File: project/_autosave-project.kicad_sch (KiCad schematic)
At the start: 6 parts, among them J1 Conn_02x16_Odd_Even, J2 USB_C_Receptacle_PowerOnly_6P, SW1 SS-12D10L9, U2 CH224K

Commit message: USB and PD circuit
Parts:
- added C1: 1u, symbol Device:C_Small
- added R1: 1K, symbol Device:R
- added R2: 10K, symbol Device:R
- added TP3: TestPoint_2Pole, symbol Connector:TestPoint_2Pole
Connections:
- net GND: now also J2.A12 (GND), J2.B12 (GND), U2.11 (GND), U2.2 (CFG2), U2.3 (CFG3), U2.9 (CFG1), C1.2
- net at J2.A5 (CC1): now also U2.7 (CC1)
- net at J2.A9 (VBUS), J2.B9 (VBUS): now also R1.2, R2.2
- net at J2.B5 (CC2): now also U2.6 (CC2)
- net VDD: now reaches U2.1 (VDD)
- net VDD: now also C1.1, R1.1
- net at U2.4 (DP): now also TP3.2
- net at U2.5 (DM): now also TP3.1
- net at U2.8 (VBUS): now also R2.1
- no-connect marks 1 -> 2
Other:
- note added: "Double pole TP added( if DM/DP needs to be shorted)"
- note added: "USB Type C and PD circuit"
- moved on the sheet: J2, U2

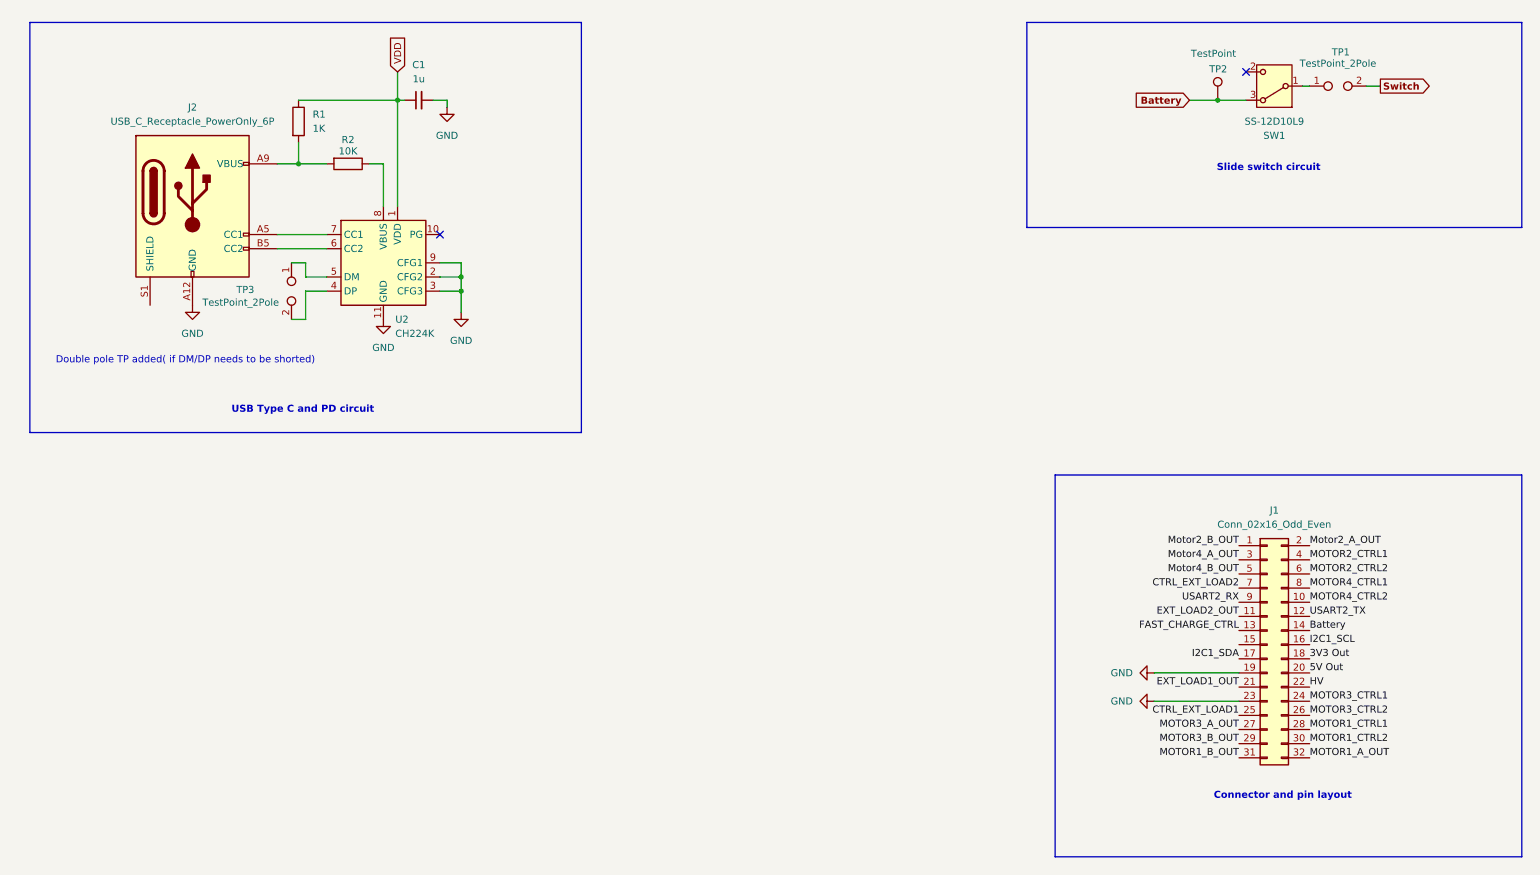
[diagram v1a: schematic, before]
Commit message: Add switching circuits
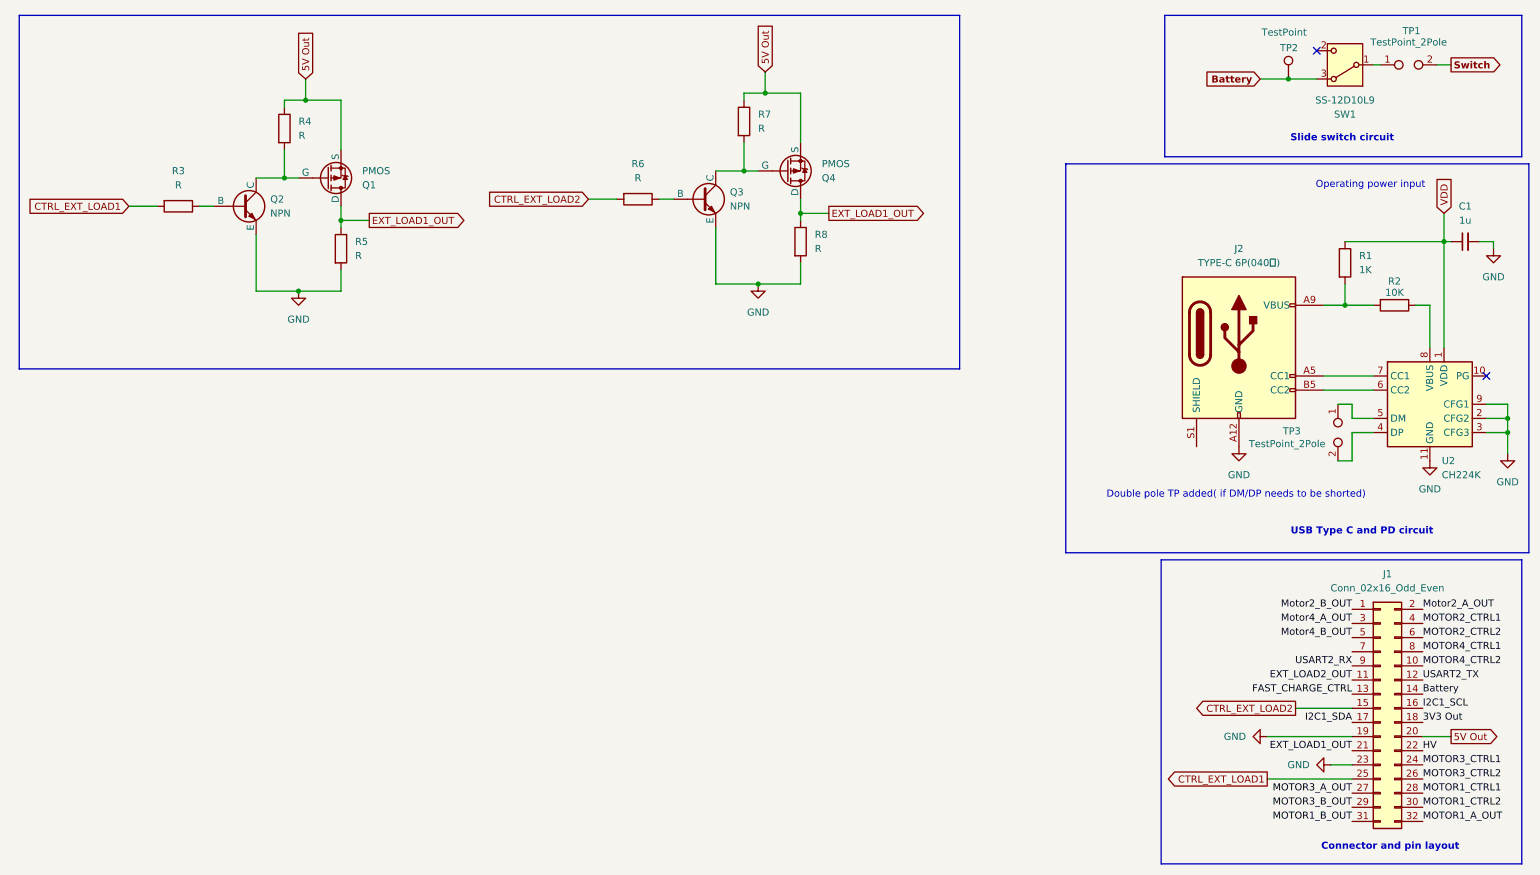
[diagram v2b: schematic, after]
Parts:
- added Q1, Q4: PMOS, symbol Simulation_SPICE:PMOS
- added Q2, Q3: NPN, symbol Simulation_SPICE:NPN
- added R3, R4, R5, R6, R7, R8: R, symbol Device:R
- J2: value USB_C_Receptacle_PowerOnly_6P -> TYPE-C 6P(040新)
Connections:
- net 5V Out: now also Q1.3 (S), Q4.3 (S), R4.1, R7.1
- net CTRL_EXT_LOAD1: now also R3.2
- net CTRL_EXT_LOAD2: now also J1.15 (Pin_15), R6.2; no longer J1.7 (Pin_7)
- net EXT_LOAD1_OUT: now also Q1.1 (D), Q4.1 (D), R5.1, R8.1
- net GND: now also Q2.3 (E), Q3.3 (E), R5.2, R8.2
- new net: Q1.2 (G), Q2.1 (C), R4.2
- new net: Q2.2 (B), R3.1
- new net: Q3.2 (B), R6.1
- new net: Q3.1 (C), Q4.2 (G), R7.2
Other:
- note added: "Operating power input"
- moved on the sheet: C1, J1, J2, R1, R2, SW1, TP1, TP2, TP3, U2

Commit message: Update _autosave-project.kicad_sch
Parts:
- renumbered R5 to R_L1, R8 to R_L2
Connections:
- net CTRL_EXT_LOAD2: now also J1.7 (Pin_7); no longer J1.15 (Pin_15)
- net EXT_LOAD1_OUT: no longer Q4.1 (D), R_L2.1
- net EXT_LOAD2_OUT: now also Q4.1 (D), R_L2.1
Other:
- note added: "External Load Switching circuits"
- note added: "Switch input?"
- moved on the sheet: Q1, Q2, Q3, Q4, R3, R4, R6, R7, R_L1, R_L2
